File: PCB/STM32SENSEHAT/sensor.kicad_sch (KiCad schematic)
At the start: 14 parts, among them U4 BME280, U5 TMP112xxDRL, U6 CAT24C256

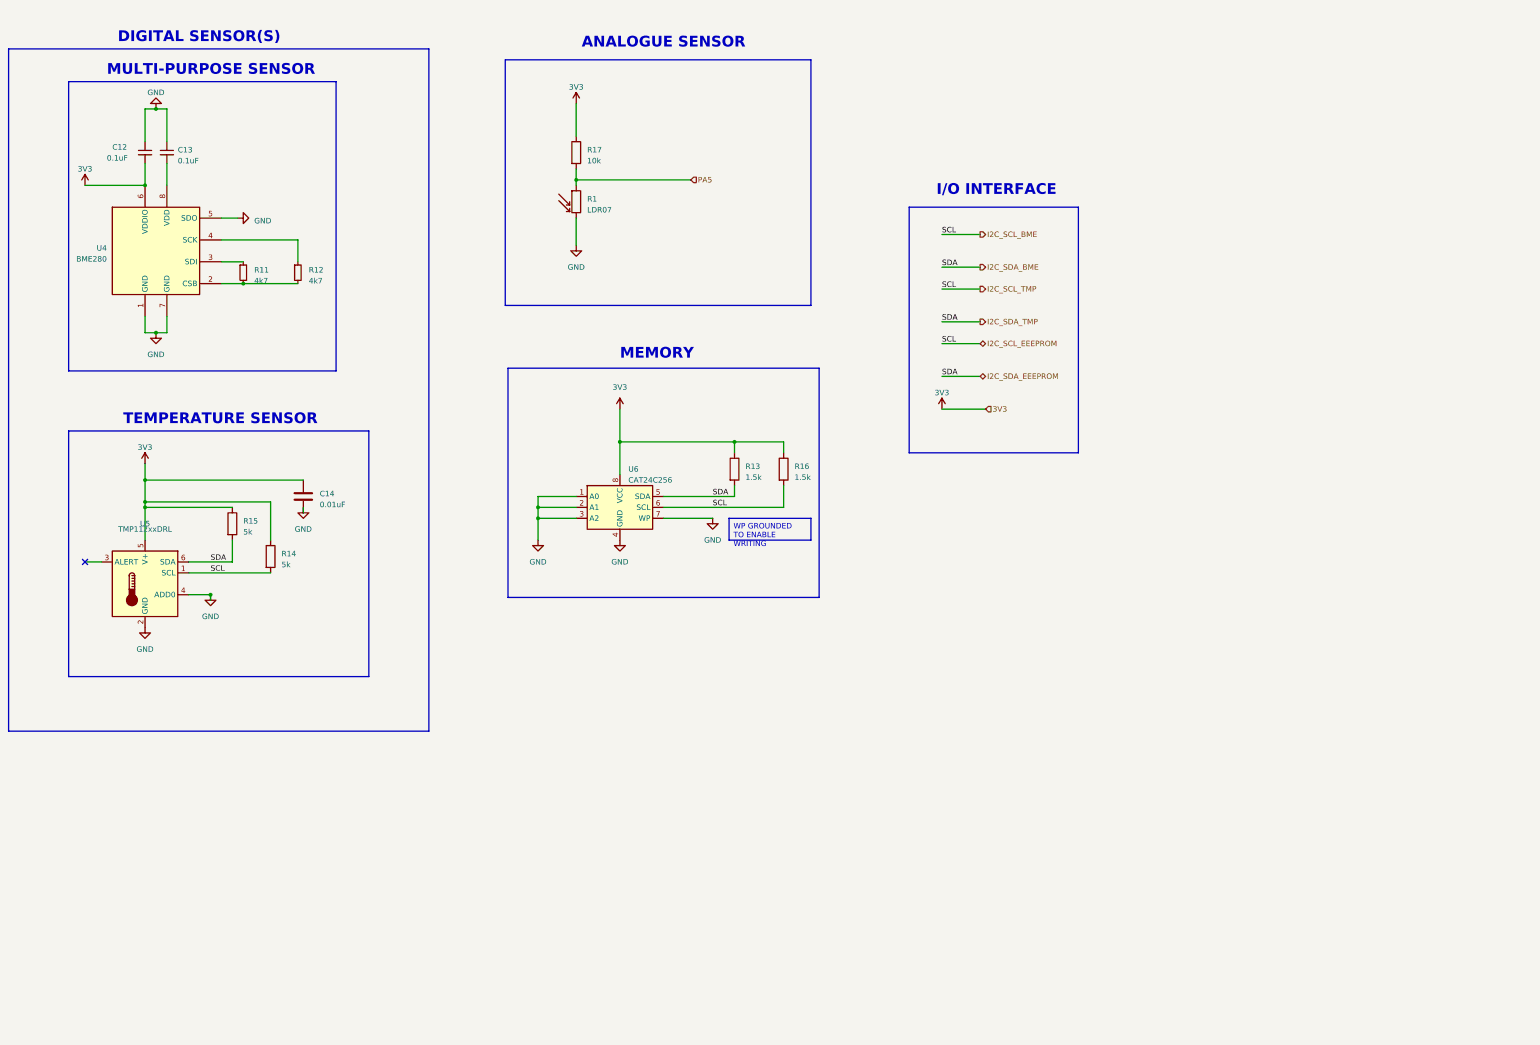
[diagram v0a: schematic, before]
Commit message: Removed the extra sensor, Modified BME280 interfacing and FTDI UART pins. Added Manual Reset to MCU and configured BOOT pin
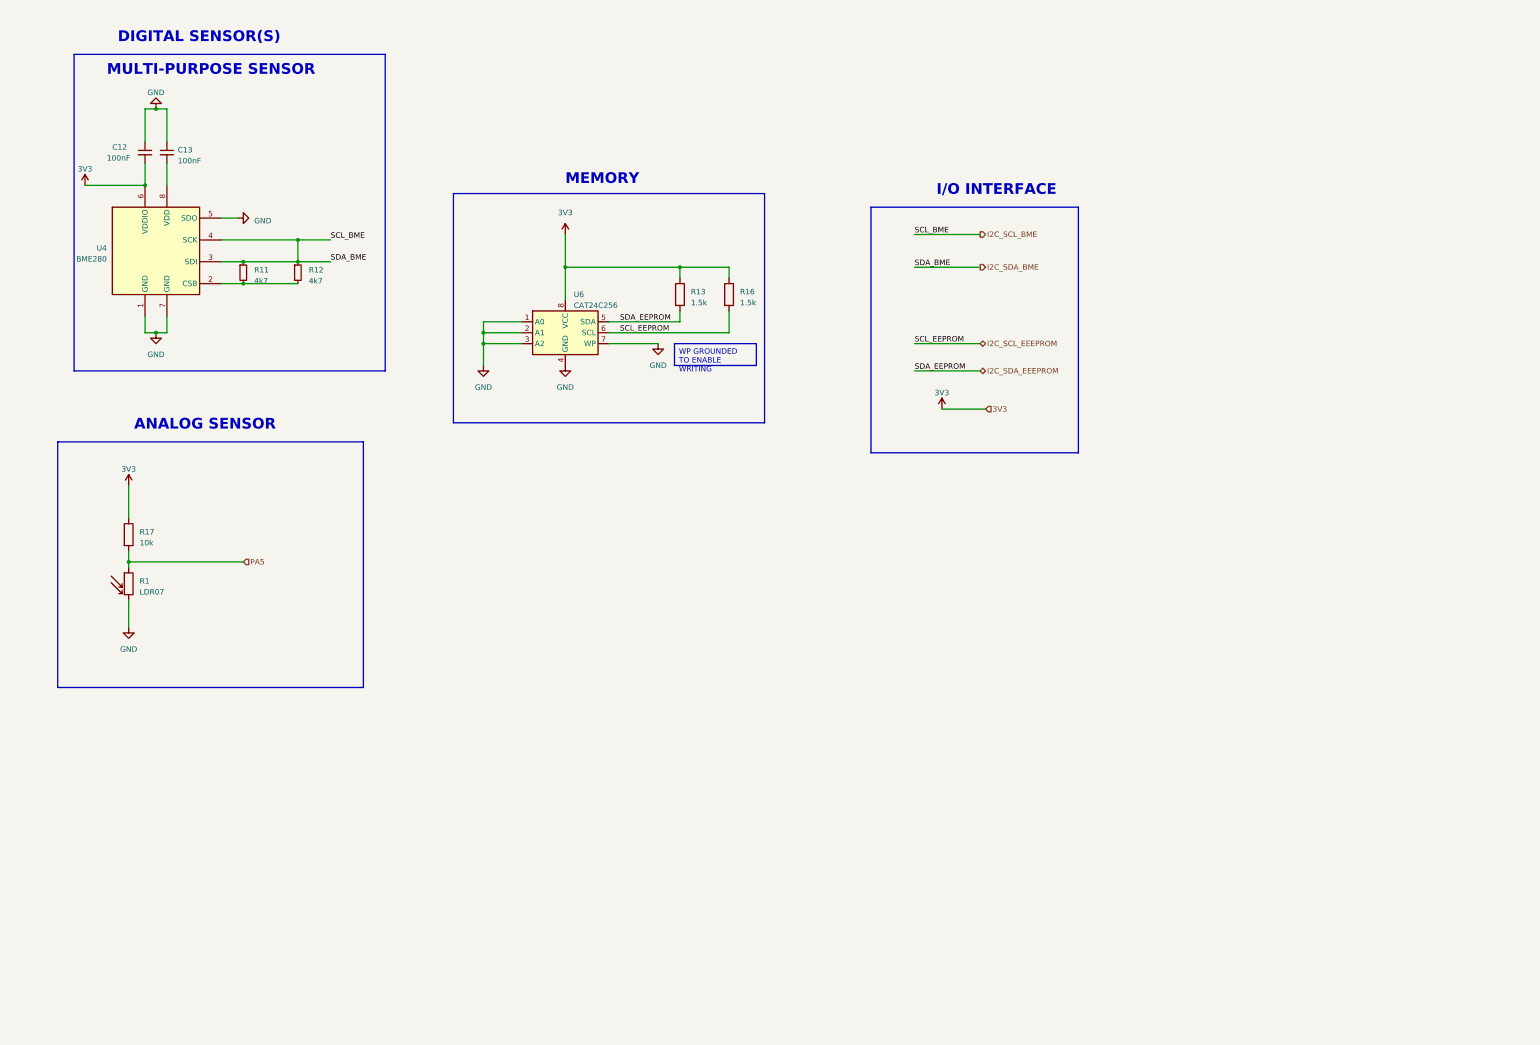
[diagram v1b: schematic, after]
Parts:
- removed C14: 0.01uF, symbol Device:C
- removed R14, R15: 5k, symbol Device:R
- removed U5: TMP112xxDRL, Package_TO_SOT_SMD:SOT-563, symbol Sensor_Temperature:TMP112xxDRL
- C12, C13: value 0.1uF -> 100nF
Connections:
- net I2C_SCL_BME: now also R11.1, R12.1, U4.3 (SDI), U4.4 (SCK); no longer R16.2, U6.6 (SCL)
- net I2C_SDA_BME renamed I2C_SDA_EEEPROM
- new net I2C_SCL_EEEPROM: R16.2, U6.6 (SCL)
- no-connect marks 1 -> 0
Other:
- note added: "ANALOG SENSOR"
- note removed: "ANALOGUE SENSOR"
- note removed: "TEMPERATURE SENSOR"
- moved on the sheet: R1, R13, R16, R17, U6

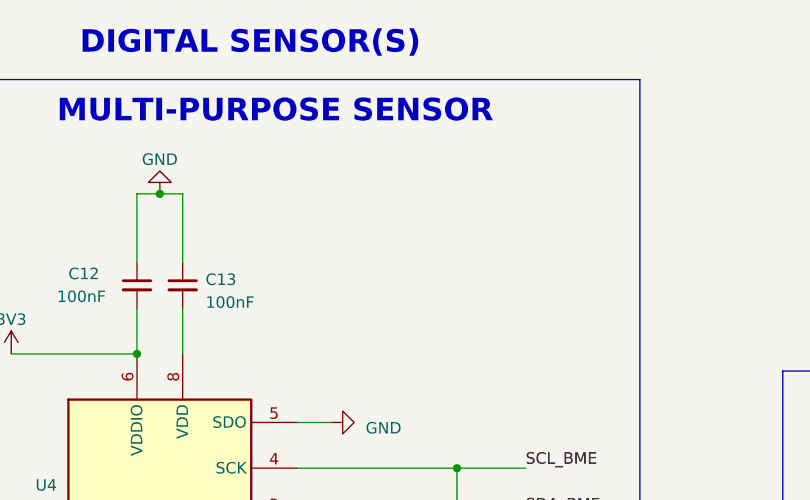
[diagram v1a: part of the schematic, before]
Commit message: Add STM32SENSEHAT, power, sensor, and mcu schematic file
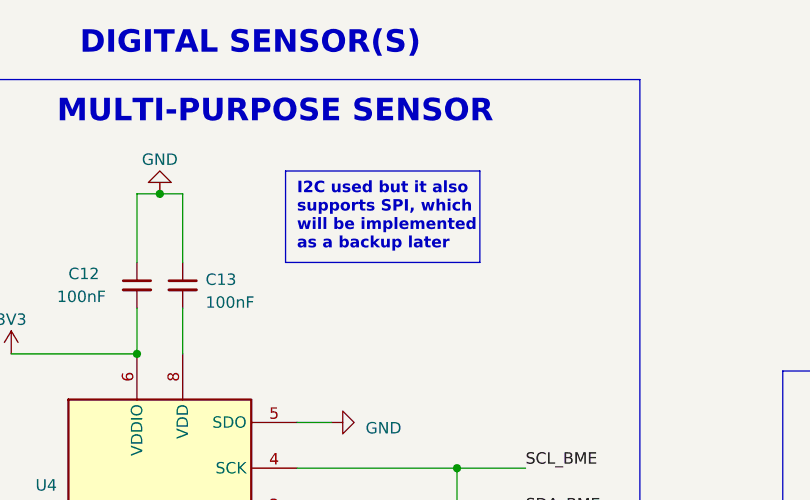
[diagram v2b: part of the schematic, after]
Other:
- note added: "I2C used but it also supports SPI, which will be implemented as a backup later"
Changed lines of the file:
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@@
+    (fill (type none))
+  )
+  (rectangle (start 72.39 36.83) (end 93.98 46.99)
+    (stroke (width 0) (type default) (color 255 0 0 1))
     (fill (type none))
   )
@@
     (effects (font (size 2.5 2.5) (thickness 0.5) bold) (justify left bottom))
   )
+  (text "I2C used but it also\nsupports SPI, which\nwill be implemented\nas a backup later"
+    (at 73.66 45.72 0)
+    (effects (font (size 1.27 1.27) (thickness 0.254) bold (color 255 0 0 1)) (justify left bottom))
+  )
   (text "MEMORY\n" (at 153.67 57.15 0)

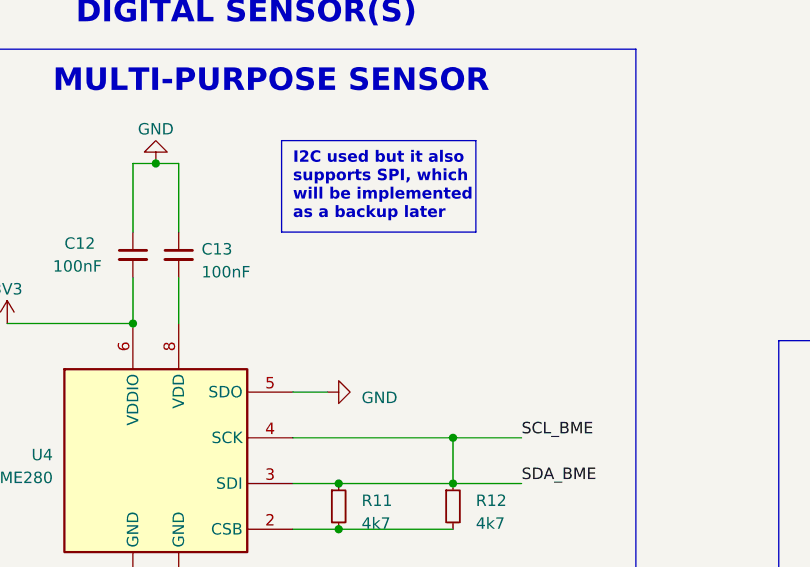
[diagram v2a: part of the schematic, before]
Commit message: Rectified management spelling, added notes to sensor module and removed extra sensor's I2C pin
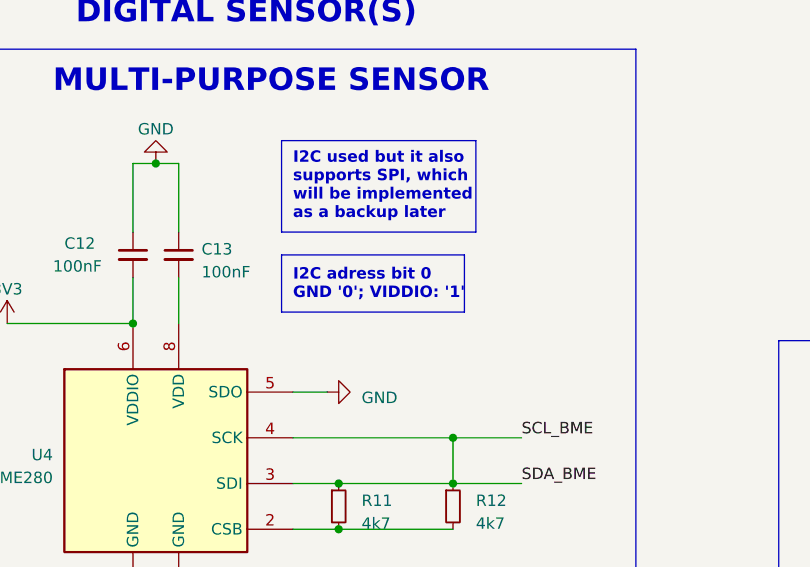
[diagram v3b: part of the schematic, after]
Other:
- note added: "I2C adress bit 0 GND '0'; VIDDIO: '1'"
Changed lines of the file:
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@@
+    (fill (type none))
+  )
+  (rectangle (start 72.39 49.53) (end 92.71 55.88)
+    (stroke (width 0) (type default) (color 255 153 0 1))
     (fill (type none))
   )
@@
     (effects (font (size 1.27 1.27) (thickness 0.254) bold (color 255 0 0 1)) (justify left bottom))
   )
+  (text "I2C adress bit 0\nGND '0'; VIDDIO: '1'\n" (at 73.66 54.61 0)
+    (effects (font (size 1.27 1.27) (thickness 0.254) bold (color 255 153 0 1)) (justify left bottom))
+  )
   (text "MEMORY\n" (at 153.67 57.15 0)

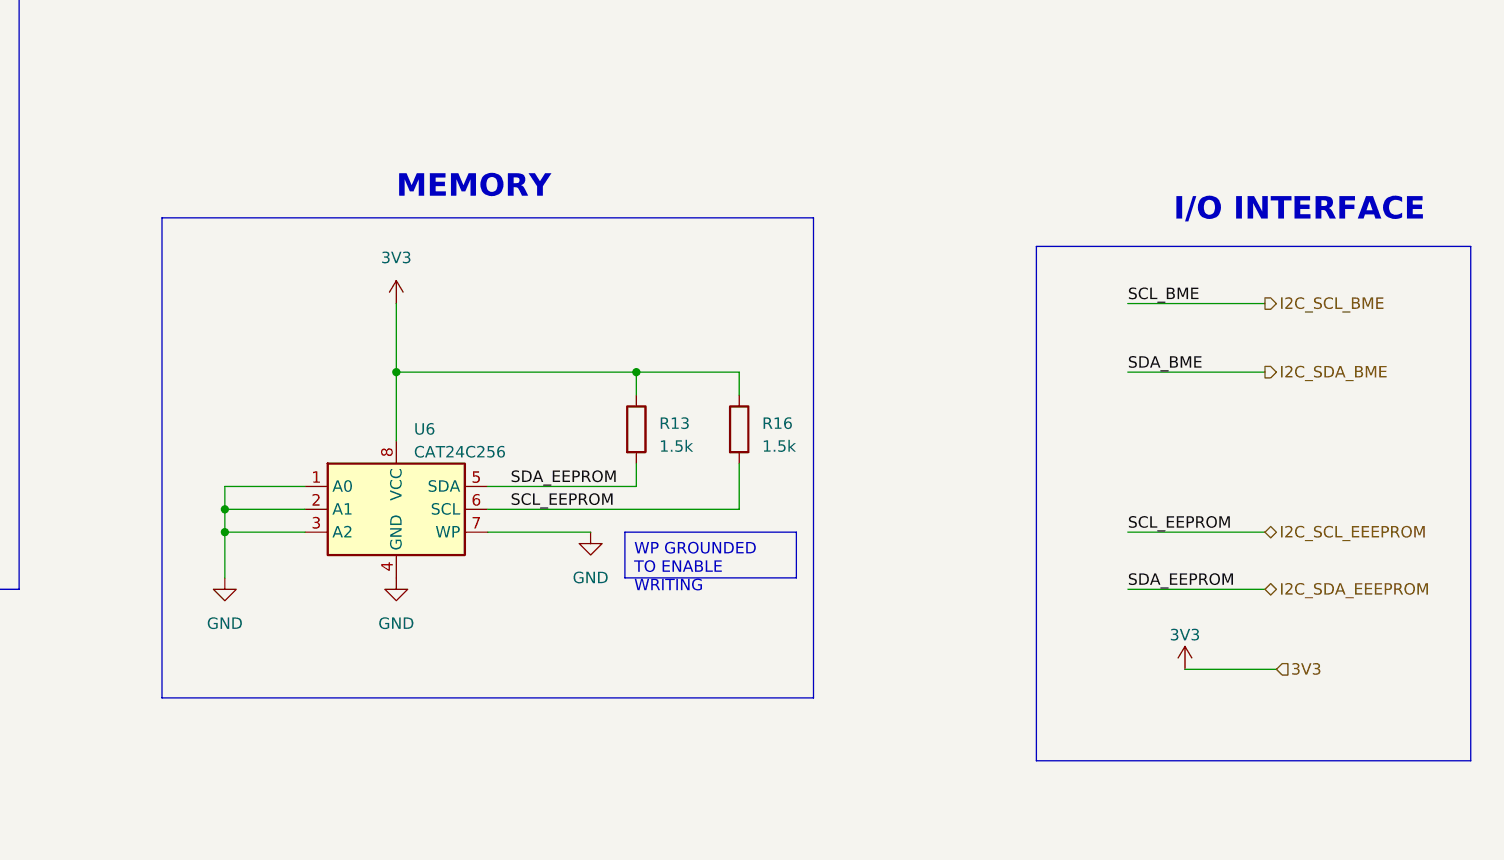
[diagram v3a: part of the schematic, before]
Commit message: Revised schematics. Moved USB and EEPROM sub modules to MCU sheet and and rectified the top sheet accordingly
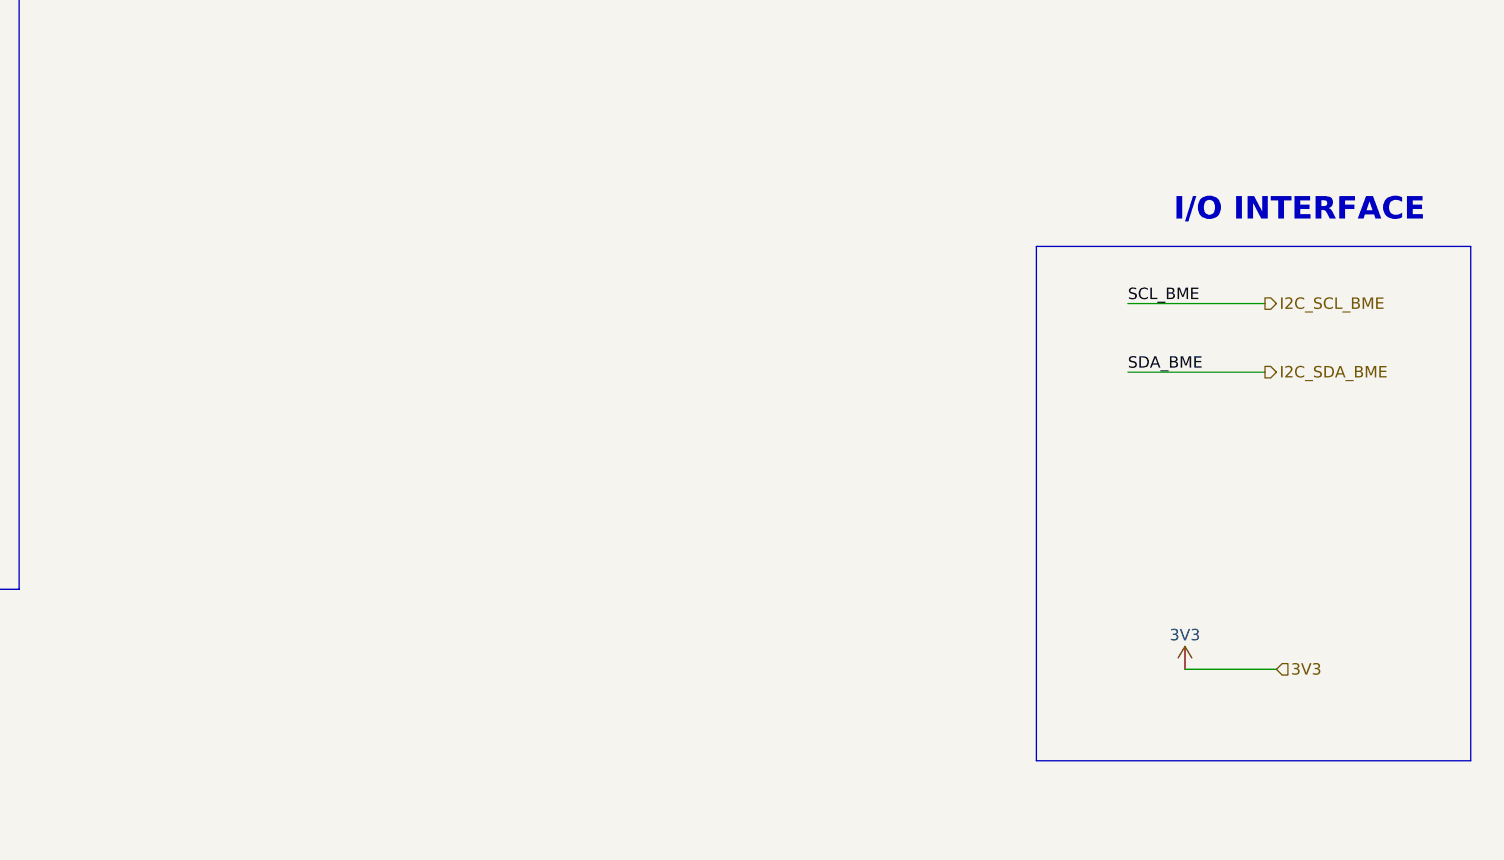
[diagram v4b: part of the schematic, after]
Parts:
- removed R13, R16: 1.5k, symbol Device:R
- removed U6: CAT24C256, symbol Memory_EEPROM:CAT24C256
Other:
- note removed: "MEMORY"
